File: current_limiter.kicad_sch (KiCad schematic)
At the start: 22 parts, among them J35 Conn_02x02, Q10 MMBT5551, Q11 LBSS84LT1G, Q9 MMBT5551, U51 COS1333TR, U52 LMV321-TR

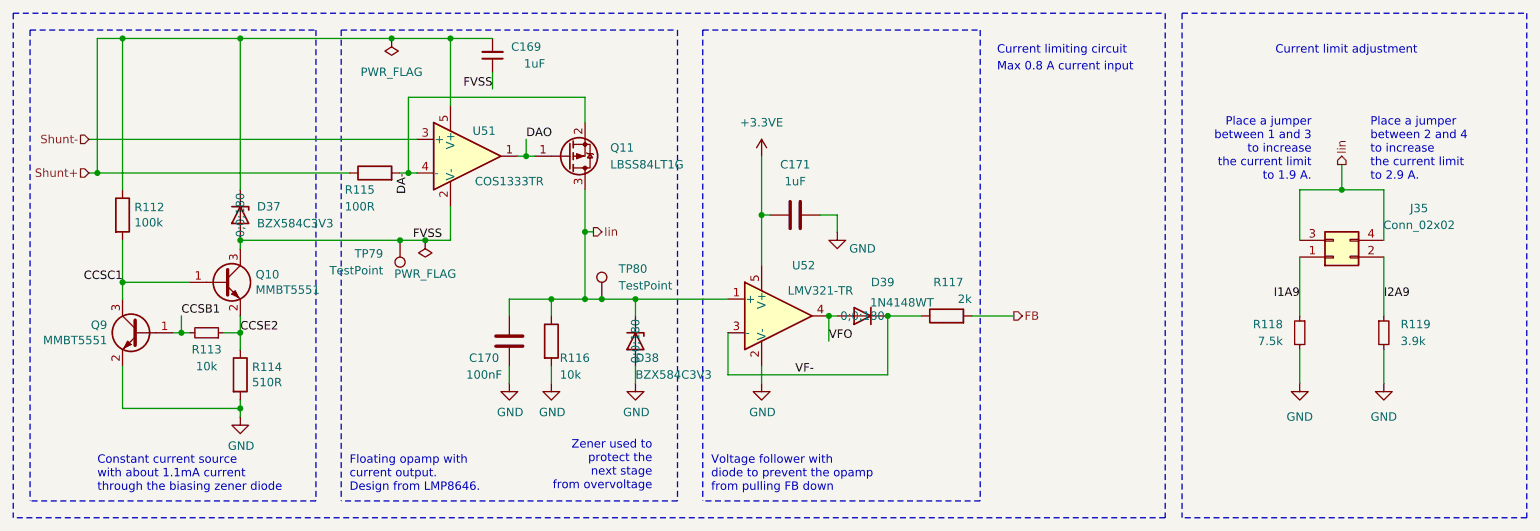
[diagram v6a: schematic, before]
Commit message: Nailed the current limiter design
Also added more GND test pads
Also fixed the MCU I2C pinout
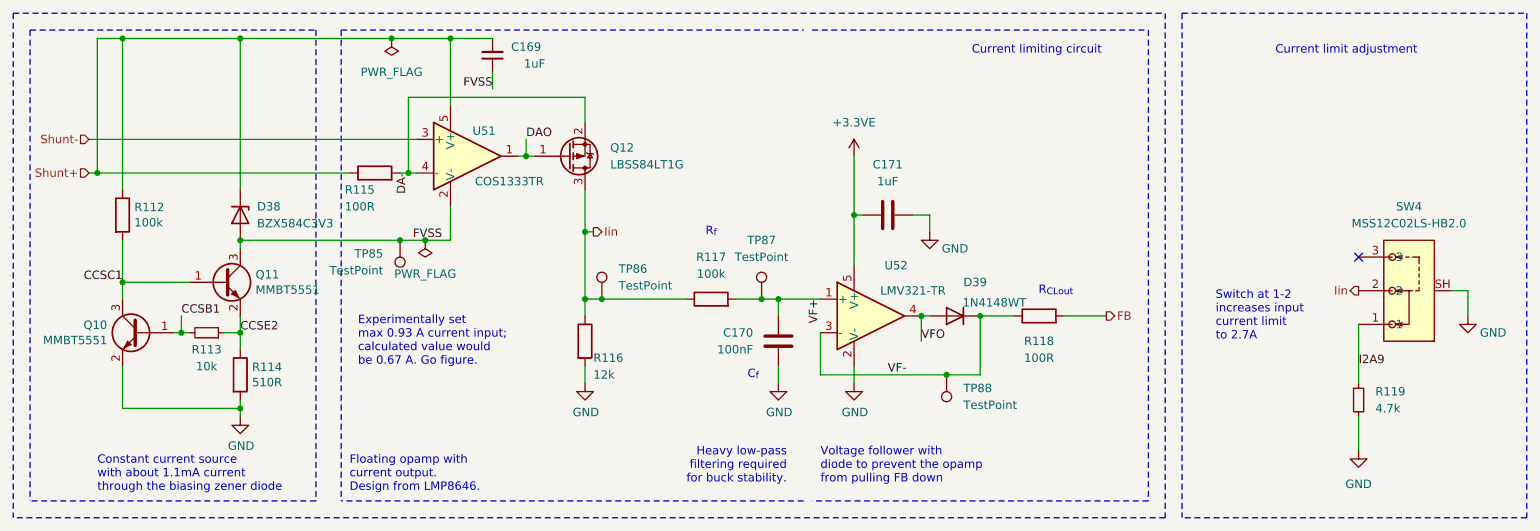
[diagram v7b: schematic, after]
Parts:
- removed D38: BZX584C3V3, Diode_SMD:D_SOD-523, symbol Device:D_Zener
- removed J35: Conn_02x02, Connector_PinHeader_2.54mm:PinHeader_2x02_P2.54mm_Vertical_SMD, symbol Connector_Generic:Conn_02x02_Odd_Even
- removed R118: 7.5k, Resistor_SMD:R_0603_1608Metric_Pad0.98x0.95mm_HandSolder, symbol Device:R_Small
- added R117: 100k, Resistor_SMD:R_0603_1608Metric_Pad0.98x0.95mm_HandSolder, symbol Device:R
- added SW4: MSS12C02LS-HB2.0, HL_Button_Switch:SW-SMD_MSS12C02LS-HB2.0-1, symbol Hatlabs:MSS12C02LS-HB2.0
- added TP87, TP88: TestPoint, TestPoint:TestPoint_Pad_D1.0mm, symbol Connector:TestPoint
- R116: value 10k -> 12k; LCSC C25804 -> C22790
- R118: renamed from R117; value 2k -> 100R; footprint Resistor_SMD:R_0603_1608Metric -> Resistor_SMD:R_0603_1608Metric_Pad0.98x0.95mm_HandSolder; LCSC C22975 -> C22775
- R119: value 3.9k -> 4.7k; LCSC C23018 -> (none)
- renumbered D37 to D38, Q9 to Q10, Q10 to Q11, Q11 to Q12, TP79 to TP85, TP80 to TP86
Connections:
- net GND: now also C170.2, SW4.SH; no longer C170.1
- net I2A9: now also SW4.1
- net Iin: now also R117.1, SW4.2; no longer C170.2, U52.1 (+)
- net VF-: now also TP88.1
- new net VF+: C170.1, R117.2, TP87.1, U52.1 (+)
- no-connect marks 0 -> 1
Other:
- note added: "C_{f}"
- note added: "Experimentally set max 0.93 A current input; calculated value would be 0.67 A. Go figure."
- note added: "Heavy low-pass filtering required for buck stability."
- note added: "R_{CLout}"
- note added: "R_{f}"
- note added: "Switch at 1-2 increases input current limit to 2.7A"
- note removed: "Max 0.8 A current input"
- note removed: "Place a jumper between 1 and 3 to increase the current limit to 1.9 A."
- note removed: "Place a jumper between 2 and 4 to increase the current limit to 2.9 A."
- note removed: "Zener used to protect the next stage from overvoltage"
- moved on the sheet: C171, D39, R116, R118, R119, U52

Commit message: Optimize 10V buck converter based on testing
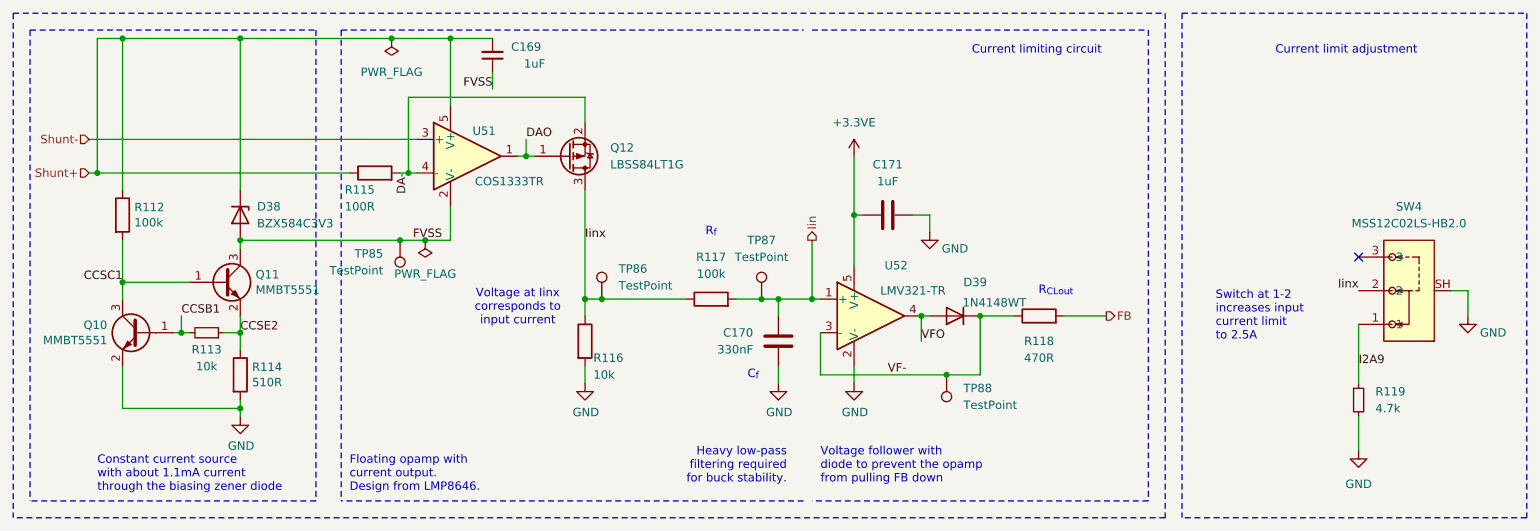
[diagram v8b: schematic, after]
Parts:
- C170: value 100nF -> 330nF; LCSC C14663 -> (none)
- R116: value 12k -> 10k; LCSC C22790 -> (none)
- R118: value 100R -> 470R; LCSC C22775 -> (none)
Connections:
- net VF+ is gone; now on net Iin: C170.1, R117.2, TP87.1, U52.1 (+)
- net Iin: no longer Q12.3 (D), R116.1, R117.1, SW4.2, TP86.1
- new net Iinx: Q12.3 (D), R116.1, R117.1, SW4.2, TP86.1
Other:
- note added: "Switch at 1-2 increases input current limit to 2.5A"
- note added: "Voltage at Iinx corresponds to input current"
- note removed: "Experimentally set max 0.93 A current input; calculated value would be 0.67 A. Go figure."
- note removed: "Switch at 1-2 increases input current limit to 2.7A"
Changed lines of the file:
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@@
 		(comment 3 "HALPI2 is licensed under CERN-OHL-S v2.")
 	)
-	(text "Switch at 1-2\nincreases input\ncurrent limit\nto 2.7A"
+	(text "Switch at 1-2\nincreases input\ncurrent limit\nto 2.5A"
 		(exclude_from_sim no)
 		(at 215.9 99.06 0)
@@
 		)
 	)
+	(text "Voltage at Iinx\ncorresponds to\ninput current"
+		(exclude_from_sim no)
+		(at 110.49 93.98 0)
+		(effects
+			(font
+				(size 1.27 1.27)
+			)
+		)
+	)
 	(text "Current limiting circuit"
 		(exclude_from_sim no)
@@
 		)
 	)
-	(text "Experimentally set\nmax 0.93 A current input;\ncalculated value would \nbe 0.67 A. Go figure."
-		(exclude_from_sim no)
-		(at 86.36 102.87 0)
-		(effects
-			(font
-				(size 1.27 1.27)
-			)
-			(justify left bottom)
-		)
-	)
 	(junction
 		(at 46.99 73.66)
@@
 	)
 	(junction
-		(at 120.65 82.55)
-		(diameter 0)
-		(color 0 0 0 0)
-	)
-	(junction
 		(at 171.45 95.25)
 		(diameter 0)
@@
 	)
 	(junction
+		(at 154.94 92.71)
+		(diameter 0)
+		(color 0 0 0 0)
+	)
+	(junction
 		(at 175.26 104.14)
 		(diameter 0)
@@
 	(wire
 		(pts
-			(xy 149.86 92.71) (xy 156.21 92.71)
+			(xy 149.86 92.71) (xy 154.94 92.71)
 		)
 		(stroke
@@
 	(wire
 		(pts
+			(xy 154.94 92.71) (xy 156.21 92.71)
+		)
+		(stroke
+			(width 0)
+			(type default)
+		)
+	)
+	(wire
+		(pts
 			(xy 171.45 95.25) (xy 171.45 99.06)
 		)
@@
 	(wire
 		(pts
-			(xy 68.58 83.82) (xy 92.71 83.82)
+			(xy 154.94 83.82) (xy 154.94 92.71)
 		)
 		(stroke
@@
 	(wire
 		(pts
-			(xy 120.65 82.55) (xy 121.92 82.55)
+			(xy 68.58 83.82) (xy 92.71 83.82)
 		)
 		(stroke
@@
 	(wire
 		(pts
-			(xy 120.65 76.2) (xy 120.65 82.55)
+			(xy 120.65 76.2) (xy 120.65 92.71)
 		)
 		(stroke
@@
 	(wire
 		(pts
-			(xy 120.65 82.55) (xy 120.65 92.71)
-		)
-		(stroke
-			(width 0)
-			(type default)
-		)
-	)
-	(wire
-		(pts
 			(xy 161.29 102.87) (xy 161.29 105.41)
 		)
@@
 		)
 	)
-	(label "VF+"
-		(at 156.21 92.71 270)
-		(effects
-			(font
-				(size 1.27 1.27)
-			)
-			(justify right bottom)
-		)
-	)
 	(label "DAO"
 		(at 111.76 68.58 0)
@@
 		)
 	)
+	(label "Iinx"
+		(at 237.49 91.44 180)
+		(effects
+			(font
+				(size 1.27 1.27)
+			)
+			(justify right bottom)
+		)
+	)
 	(label "FVSS"
 		(at 99.06 83.82 180)
@@
 		)
 	)
+	(label "Iinx"
+		(at 120.65 83.82 0)
+		(effects
+			(font
+				(size 1.27 1.27)
+			)
+			(justify left bottom)
+		)
+	)
 	(hierarchical_label "Iin"
 		(shape output)
-		(at 121.92 82.55 0)
+		(at 154.94 83.82 90)
 		(effects
 			(font
@@
 		)
 	)
-	(hierarchical_label "Iin"
-		(shape output)
-		(at 237.49 91.44 180)
-		(effects
-			(font
-				(size 1.27 1.27)
-			)
-			(justify right)
-		)
-	)
 	(hierarchical_label "FB"
 		(shape output)
@@
 			)
 		)
-		(property "Value" "12k"
+		(property "Value" "10k"
 			(at 121.92 104.14 0)
 			(effects
@@
 			)
 		)
-		(property "LCSC" "C22790"
+		(property "LCSC" ""
 			(at 120.65 99.06 0)
 			(effects
@@
 			)
 		)
-		(property "Value" "100nF"
+		(property "Value" "330nF"
 			(at 146.05 100.3299 0)
 			(effects
@@
 			)
 		)
-		(property "LCSC" "C14663"
+		(property "LCSC" ""
 			(at 149.86 99.06 0)
 			(effects
@@
 			)
 		)
-		(property "Value" "100R"
+		(property "Value" "470R"
 			(at 189.23 101.6 90)
 			(effects
@@
 			)
 		)
-		(property "LCSC" "C22775"
+		(property "LCSC" ""
 			(at 189.23 95.25 0)
 			(effects
